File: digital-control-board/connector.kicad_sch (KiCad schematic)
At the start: 1 part

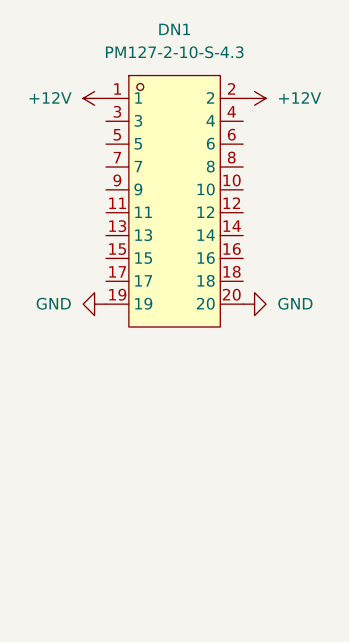
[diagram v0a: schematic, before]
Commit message: Change INA back to 25V/V, change diff gain to 1:40
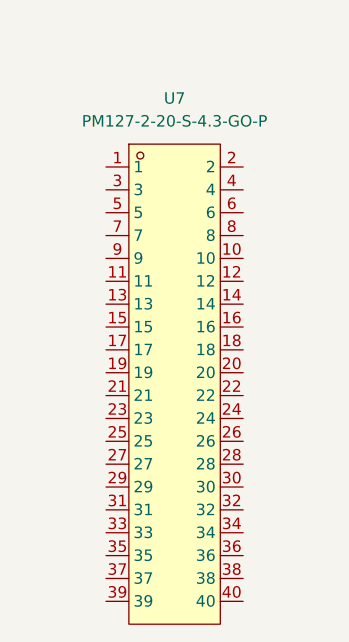
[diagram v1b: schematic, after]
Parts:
- removed DN1: PM127-2-10-S-4.3, programmable-load-library:HDR-SMD_20P-P1.27-V-F-R2-C10-LS4.8, symbol programmable-load-library:PM127-2-10-S-4.3
- added U7: PM127-2-20-S-4.3-GO-P, programmable-load-library:HDR-SMD_40P-P1.27_PM127-2-20-S-4.3-GO-P, symbol programmable-load-library:PM127-2-20-S-4.3-GO-P
